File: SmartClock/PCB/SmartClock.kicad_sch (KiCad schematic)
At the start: 3 parts, among them SW1 SW_Push, U2 XIAO-ESP32-C3-DIP

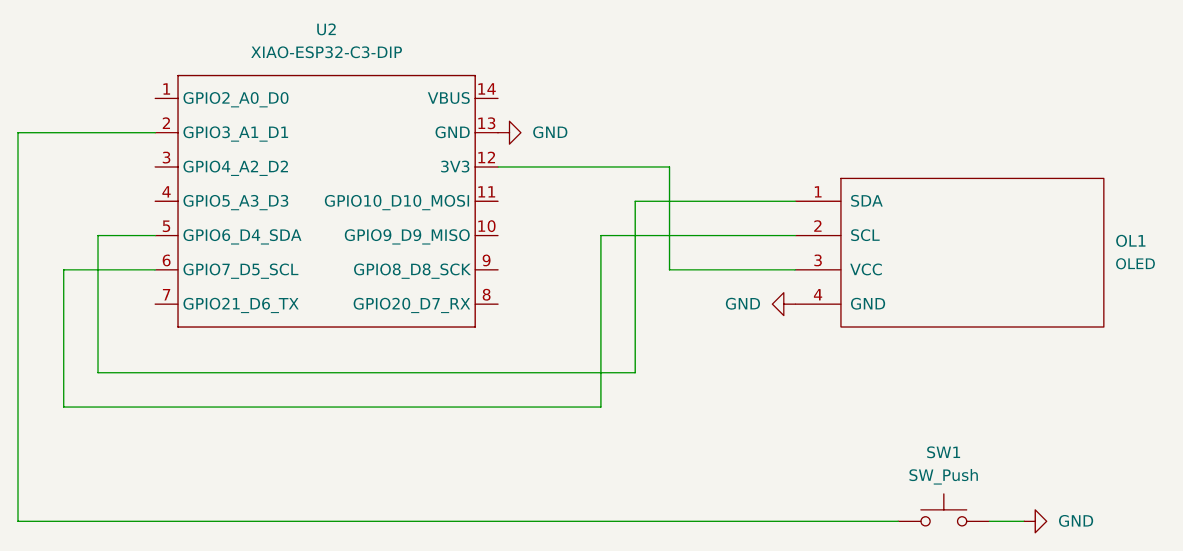
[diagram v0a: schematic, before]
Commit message: fixed pins
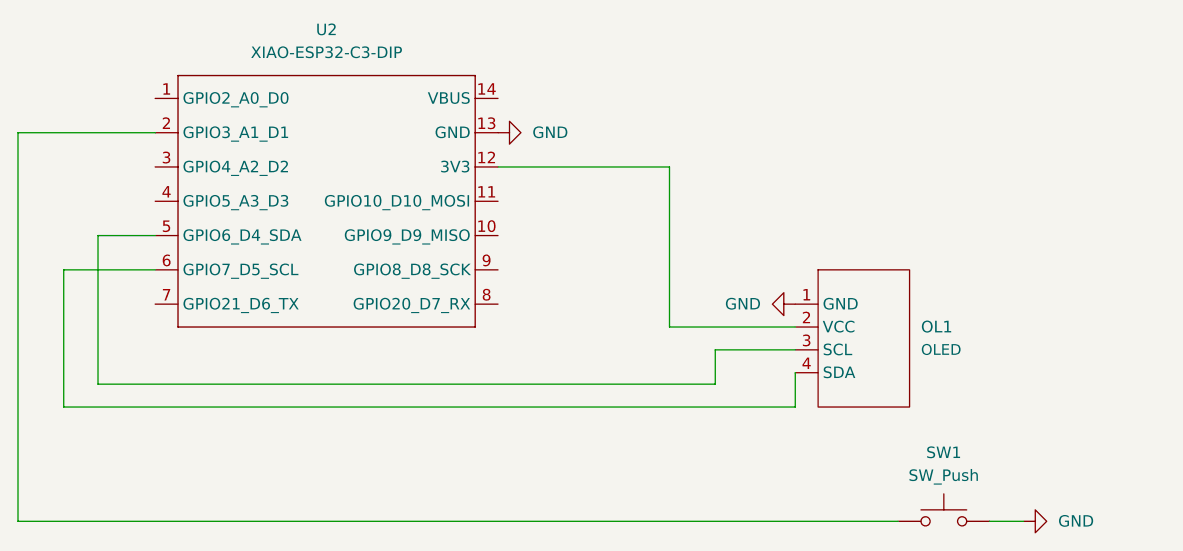
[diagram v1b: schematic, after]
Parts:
- OL1: symbol OLED2:OLED -> Buki:SD1306
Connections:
- net GND: now also OL1.1 (GND); no longer OL1.4 (GND)
- net at U2.12 (3V3): now also OL1.2 (VCC); no longer OL1.3 (VCC)
- net at U2.5 (GPIO6_D4_SDA): now also OL1.3 (SCL); no longer OL1.1 (SDA)
- net at U2.6 (GPIO7_D5_SCL): now also OL1.4 (SDA); no longer OL1.2 (SCL)
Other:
- moved on the sheet: OL1
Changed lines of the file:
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@@
 	(wire
 		(pts
-			(xy 128.27 50.8) (xy 110.49 50.8)
-		)
-		(stroke
-			(width 0)
-			(type default)
-		)
-	)
-	(wire
-		(pts
-			(xy 110.49 50.8) (xy 110.49 69.85)
-		)
-		(stroke
-			(width 0)
-			(type default)
-		)
-	)
-	(wire
-		(pts
-			(xy 128.27 54.61) (xy 106.68 54.61)
-		)
-		(stroke
-			(width 0)
-			(type default)
-		)
-	)
-	(wire
-		(pts
-			(xy 106.68 54.61) (xy 106.68 73.66)
+			(xy 114.3 46.99) (xy 114.3 64.77)
+		)
+		(stroke
+			(width 0)
+			(type default)
+		)
+	)
+	(wire
+		(pts
+			(xy 114.3 64.77) (xy 128.27 64.77)
+		)
+		(stroke
+			(width 0)
+			(type default)
+		)
+	)
+	(wire
+		(pts
+			(xy 128.27 73.66) (xy 128.27 69.85)
+		)
+		(stroke
+			(width 0)
+			(type default)
+		)
+	)
+	(wire
+		(pts
+			(xy 119.38 71.12) (xy 119.38 67.31)
 		)
 		(stroke
@@
 	(wire
 		(pts
-			(xy 114.3 58.42) (xy 114.3 46.99)
-		)
-		(stroke
-			(width 0)
-			(type default)
-		)
-	)
-	(wire
-		(pts
 			(xy 46.99 73.66) (xy 46.99 58.42)
 		)
@@
 	(wire
 		(pts
-			(xy 50.8 69.85) (xy 50.8 54.61)
+			(xy 119.38 67.31) (xy 128.27 67.31)
+		)
+		(stroke
+			(width 0)
+			(type default)
+		)
+	)
+	(wire
+		(pts
+			(xy 50.8 71.12) (xy 50.8 54.61)
 		)
 		(stroke
@@
 	(wire
 		(pts
-			(xy 106.68 73.66) (xy 46.99 73.66)
-		)
-		(stroke
-			(width 0)
-			(type default)
-		)
-	)
-	(wire
-		(pts
-			(xy 110.49 69.85) (xy 50.8 69.85)
-		)
-		(stroke
-			(width 0)
-			(type default)
-		)
-	)
-	(wire
-		(pts
-			(xy 128.27 58.42) (xy 114.3 58.42)
+			(xy 46.99 73.66) (xy 128.27 73.66)
+		)
+		(stroke
+			(width 0)
+			(type default)
+		)
+	)
+	(wire
+		(pts
+			(xy 50.8 71.12) (xy 119.38 71.12)
 		)
 		(stroke
@@
 	)
 	(symbol
-		(lib_id "OLED2:OLED")
-		(at 147.32 57.15 0)
+		(lib_id "Buki:SD1306")
+		(at 130.81 73.66 0)
 		(unit 1)
 		(exclude_from_sim no)
@@
 		(fields_autoplaced yes)
 		(property "Reference" "OL1"
-			(at 163.83 55.245 0)
+			(at 142.24 64.77 0)
 			(effects
 				(font
@@
 		)
 		(property "Value" "OLED"
-			(at 163.83 57.785 0)
+			(at 142.24 67.31 0)
 			(effects
 				(font
@@
 		)
 		(property "Footprint" "OLED3:MODULE_DM-OLED096-636"
-			(at 147.32 54.61 0)
-			(effects
-				(font
-					(size 1.524 1.524)
+			(at 130.81 73.66 0)
+			(effects
+				(font
+					(size 1.27 1.27)
 				)
 				(hide yes)
@@
 		)
 		(property "Datasheet" ""
-			(at 147.32 54.61 0)
-			(effects
-				(font
-					(size 1.524 1.524)
+			(at 130.81 73.66 0)
+			(effects
+				(font
+					(size 1.27 1.27)
 				)
 				(hide yes)
@@
 		)
 		(property "Description" ""
-			(at 147.32 57.15 0)
-			(effects
-				(font
+			(at 130.81 73.66 0)
+			(effects
+				(font
